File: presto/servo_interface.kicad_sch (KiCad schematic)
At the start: 0 parts

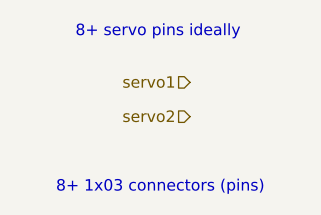
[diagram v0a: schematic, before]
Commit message: Minor document changes
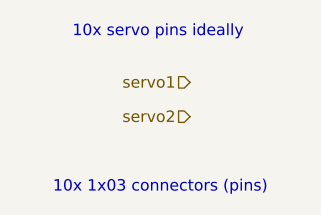
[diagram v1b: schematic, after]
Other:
- note added: "10x 1x03 connectors (pins)"
- note added: "10x servo pins ideally"
- note removed: "8+ 1x03 connectors (pins)"
- note removed: "8+ servo pins ideally"
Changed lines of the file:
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@@
 	(generator_version "9.0")
 	(paper "A4")
-	(text "8+ 1x03 connectors (pins)"
+	(text "10x 1x03 connectors (pins)"
 		(exclude_from_sim no)
 		(at 52.578 65.024 0)
@@
 		)
 	)
-	(text "8+ servo pins ideally\n"
+	(text "10x servo pins ideally\n"
 		(exclude_from_sim no)
 		(at 52.324 47.752 0)

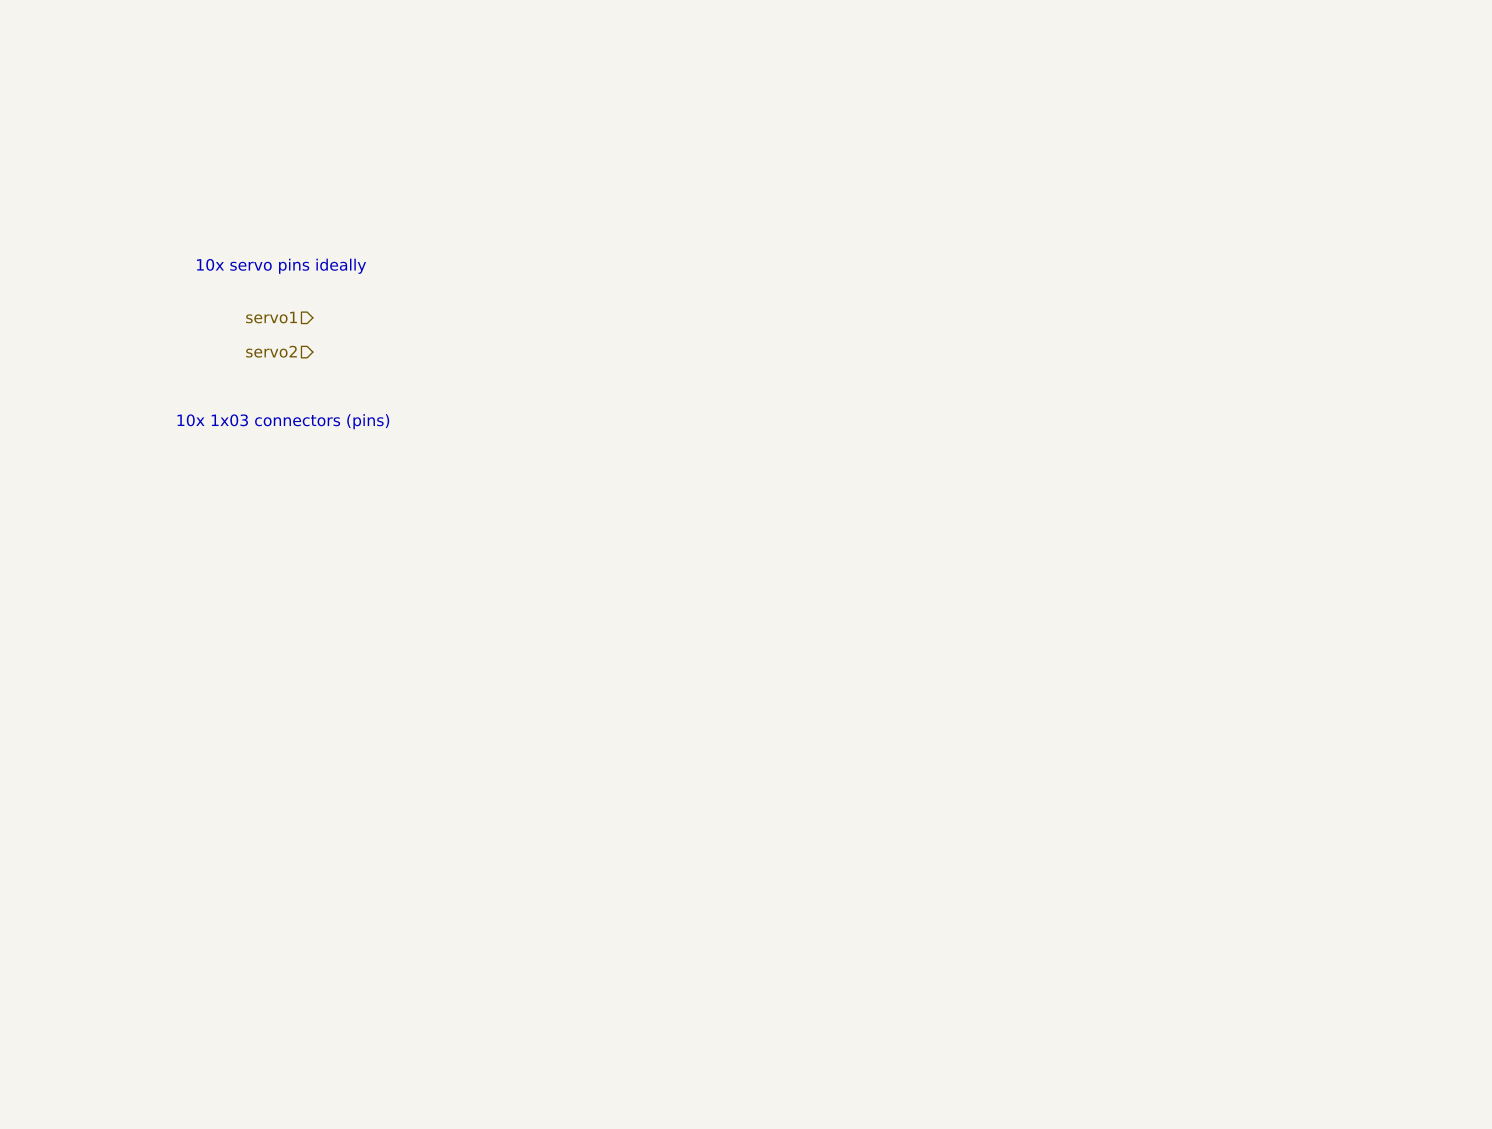
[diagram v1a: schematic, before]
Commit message: RC and Servo interface schematic done
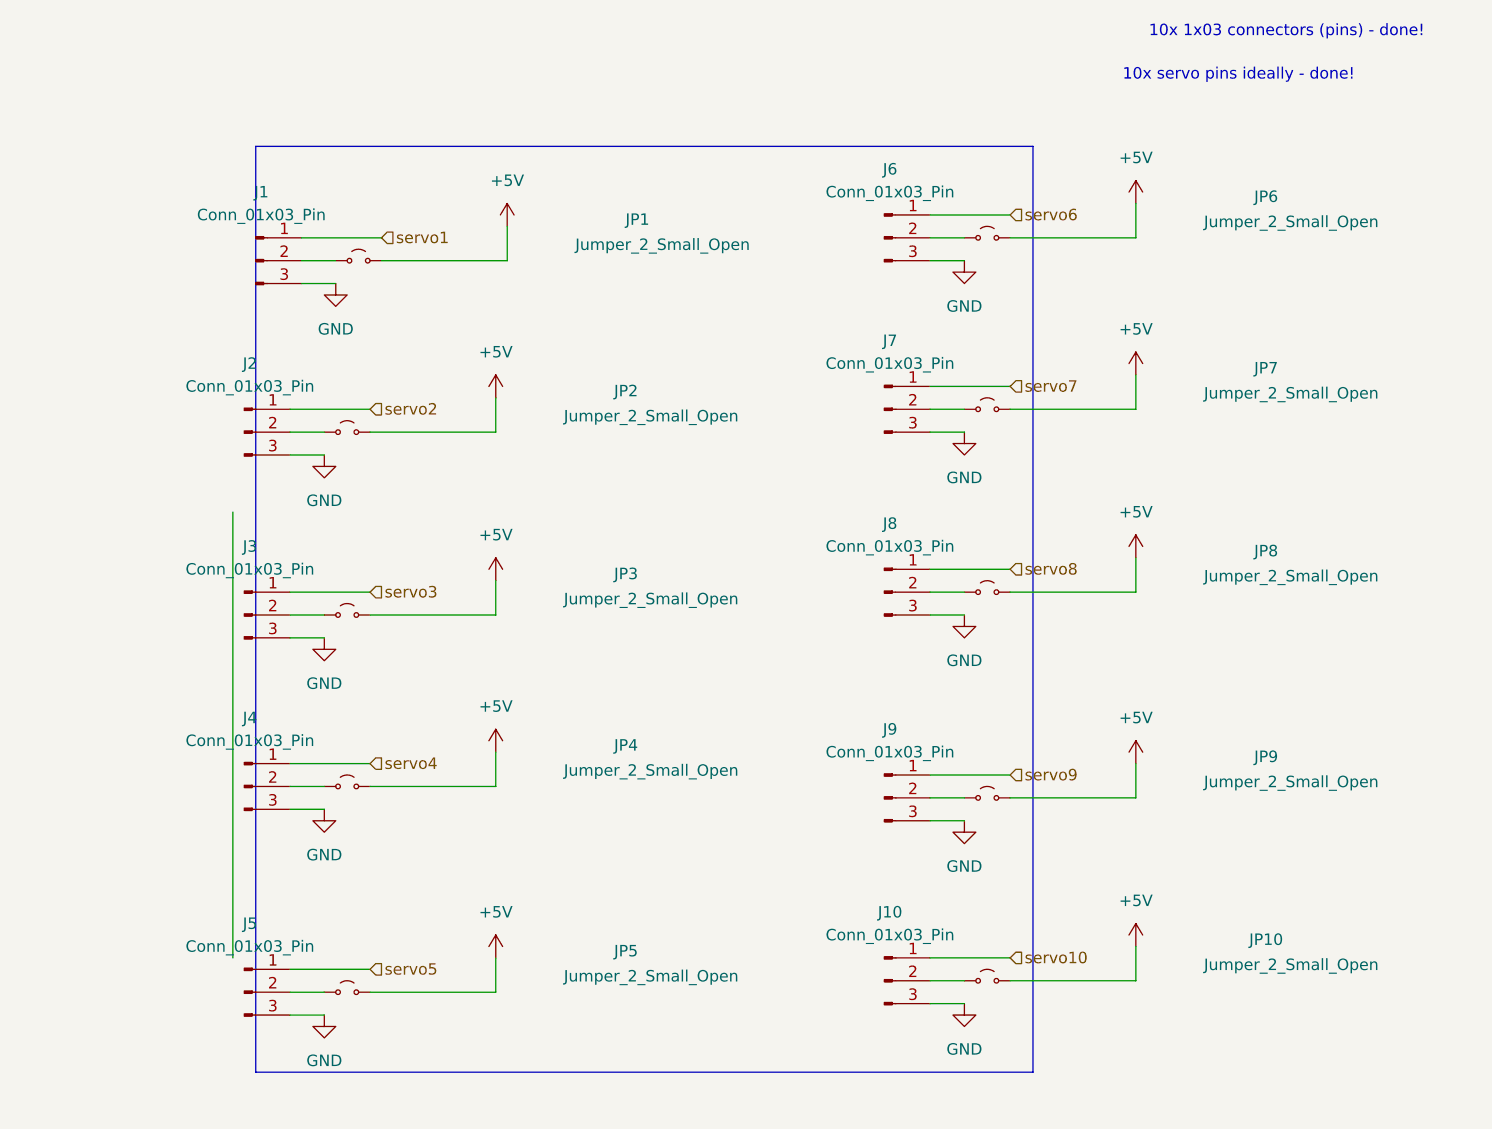
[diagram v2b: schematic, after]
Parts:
- added J1, J10, J2, J3, J4, J5, J6, J7, J8, J9: Conn_01x03_Pin, Connector_PinHeader_2.54mm:PinHeader_1x03_P2.54mm_Vertical, symbol Connector:Conn_01x03_Pin
- added JP1, JP10, JP2, JP3, JP4, JP5, JP6, JP7, JP8, JP9: Jumper_2_Small_Open, Jumper:SolderJumper-2_P1.3mm_Open_RoundedPad1.0x1.5mm, symbol Jumper:Jumper_2_Small_Open
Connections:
- net servo1: now also J1.1 (Pin_1)
- net servo2: now also J2.1 (Pin_1)
- new net: J10.2 (Pin_2), JP10.1 (A)
- new net: J8.2 (Pin_2), JP8.1 (A)
- new net: J9.2 (Pin_2), JP9.1 (A)
- new net: J3.2 (Pin_2), JP3.1 (A)
- new net: J2.2 (Pin_2), JP2.1 (A)
- new net: J6.2 (Pin_2), JP6.1 (A)
- new net: J7.2 (Pin_2), JP7.1 (A)
- new net: J4.2 (Pin_2), JP4.1 (A)
- new net: J1.2 (Pin_2), JP1.1 (A)
- new net: J5.2 (Pin_2), JP5.1 (A)
- new net +5V: JP1.2 (B), JP10.2 (B), JP2.2 (B), JP3.2 (B), JP4.2 (B), JP5.2 (B), JP6.2 (B), JP7.2 (B), JP8.2 (B), JP9.2 (B)
- new net GND: J1.3 (Pin_3), J10.3 (Pin_3), J2.3 (Pin_3), J3.3 (Pin_3), J4.3 (Pin_3), J5.3 (Pin_3), J6.3 (Pin_3), J7.3 (Pin_3), J8.3 (Pin_3), J9.3 (Pin_3)
- new net servo10: J10.1 (Pin_1)
- new net servo3: J3.1 (Pin_1)
- new net servo4: J4.1 (Pin_1)
- new net servo5: J5.1 (Pin_1)
- new net servo6: J6.1 (Pin_1)
- new net servo7: J7.1 (Pin_1)
- new net servo8: J8.1 (Pin_1)
- new net servo9: J9.1 (Pin_1)
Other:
- note added: "10x 1x03 connectors (pins) - done!"
- note added: "10x servo pins ideally - done!"
- note removed: "10x 1x03 connectors (pins)"
- note removed: "10x servo pins ideally"

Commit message: Added estop, power, led schematics
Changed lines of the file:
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@@
 	(paper "A4")
 	(rectangle
-		(start 49.53 34.29)
-		(end 135.89 137.16)
+		(start 23.114 30.988)
+		(end 180.34 141.478)
 		(stroke
 			(width 0)
@@
 		)
 		(stroke
-			(width 0)
-			(type default)
-		)
-	)
-	(wire
-		(pts
-			(xy 46.99 74.93) (xy 46.99 124.46)
-		)
-		(stroke

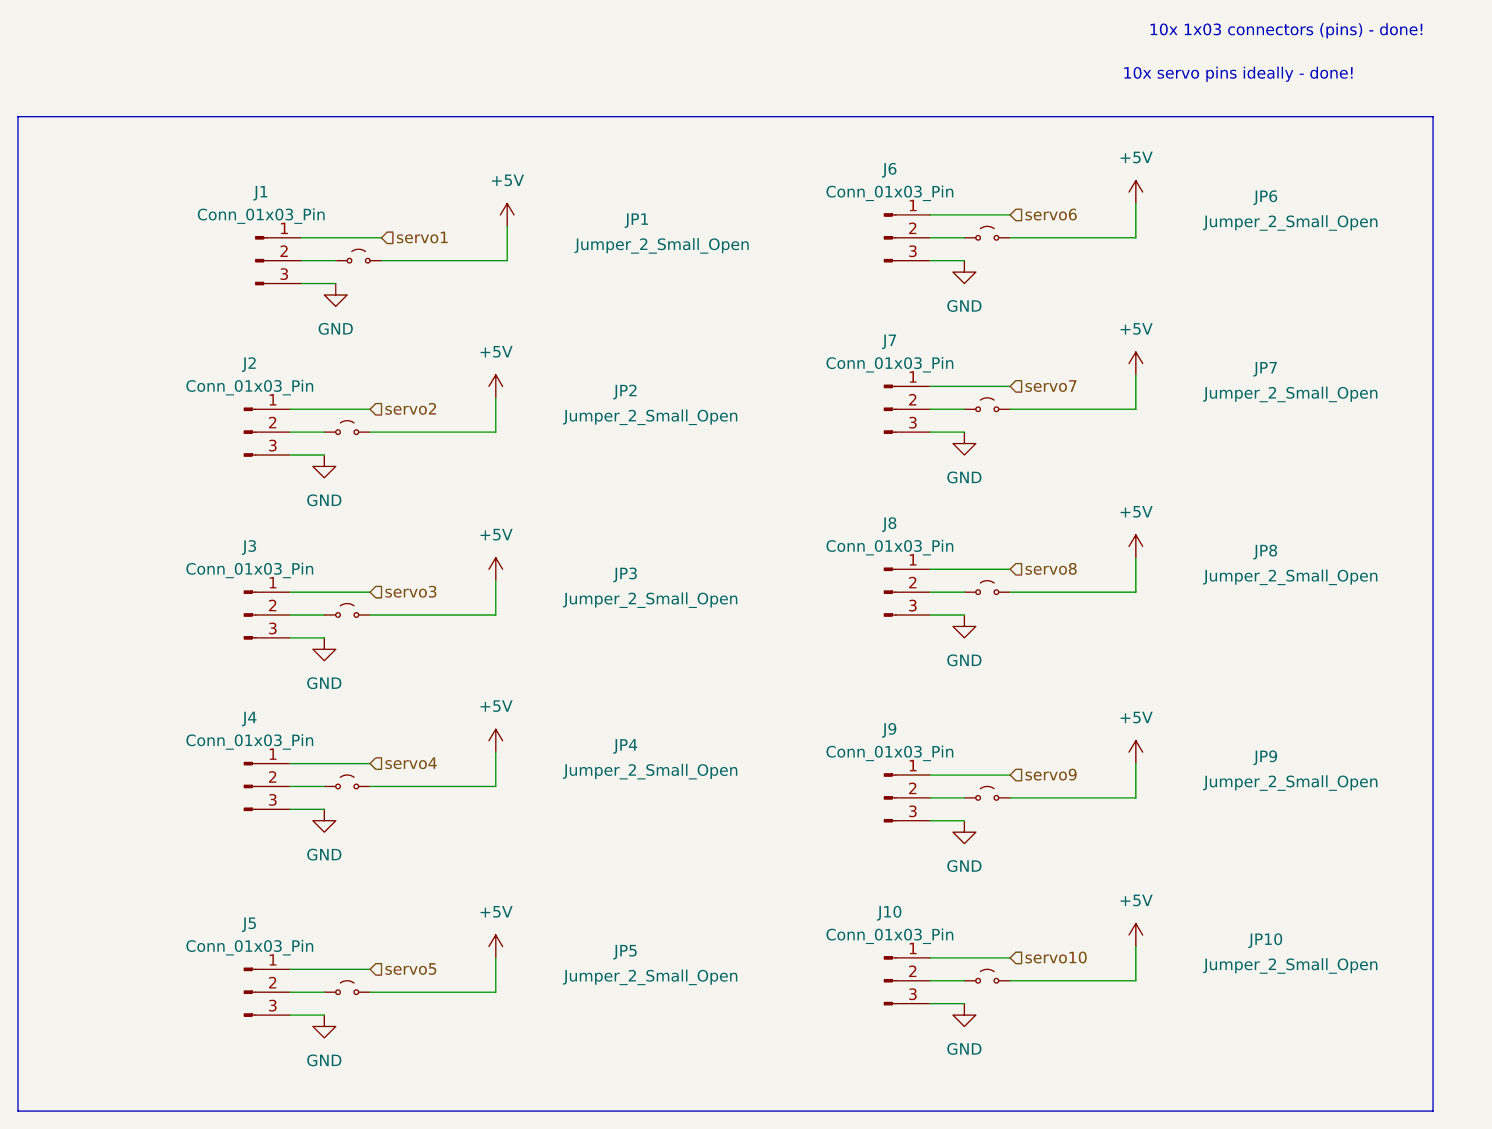
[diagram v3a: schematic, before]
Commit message: Presto PCB edited with schematic, components placed, wiring in progress
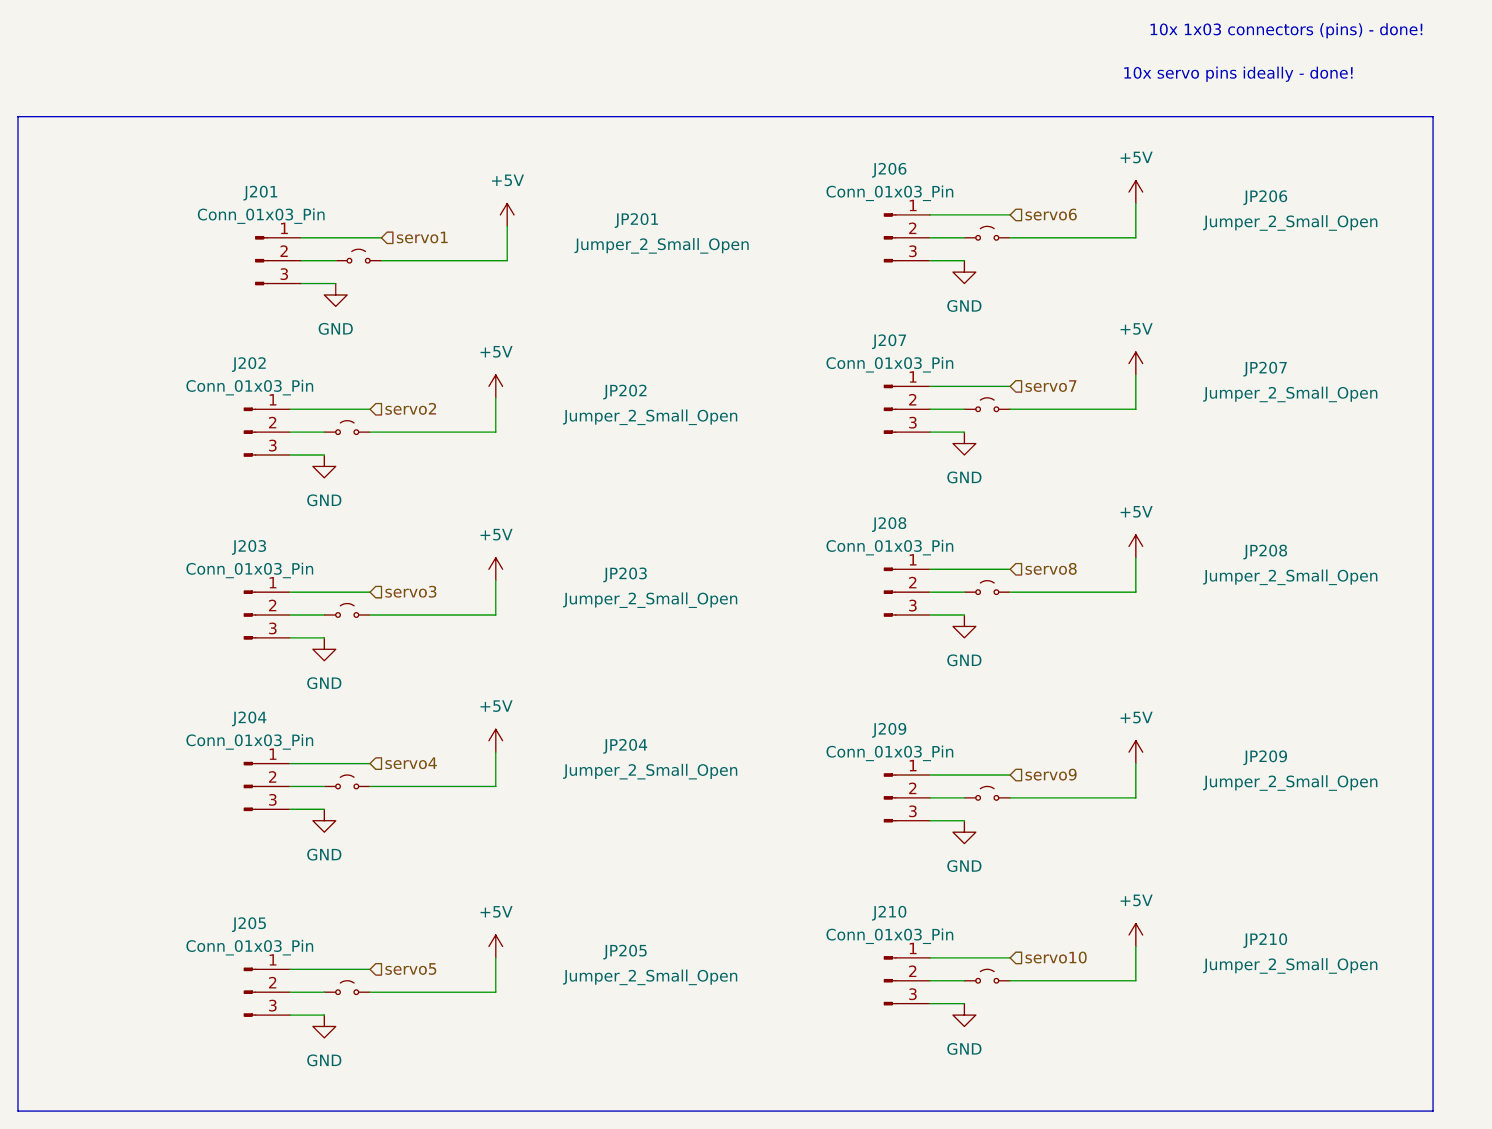
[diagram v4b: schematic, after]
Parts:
- renumbered J1 to J201, J2 to J202, J3 to J203, J4 to J204, J5 to J205, J6 to J206, J7 to J207, J8 to J208, J9 to J209, J10 to J210, JP1 to JP201, JP2 to JP202, JP3 to JP203, JP4 to JP204, JP5 to JP205, JP6 to JP206, JP7 to JP207, JP8 to JP208, JP9 to JP209, JP10 to JP210

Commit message: Rearranged to accomodate JST
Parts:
- J201, J202, J203, J204, J205, J206, J207, J208, J209, J210: footprint Connector_PinHeader_2.54mm:PinHeader_1x03_P2.54mm_Vertical -> Connector_JST:JST_XH_B3B-XH-A_1x03_P2.50mm_Vertical
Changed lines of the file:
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@@
 			)
 		)
-		(property "Footprint" "Connector_PinHeader_2.54mm:PinHeader_1x03_P2.54mm_Vertical"
+		(property "Footprint" "Connector_JST:JST_XH_B3B-XH-A_1x03_P2.50mm_Vertical"
 			(at 48.26 86.36 0)
 			(effects
@@
 			)
 		)
-		(property "Footprint" "Connector_PinHeader_2.54mm:PinHeader_1x03_P2.54mm_Vertical"
+		(property "Footprint" "Connector_JST:JST_XH_B3B-XH-A_1x03_P2.50mm_Vertical"
 			(at 48.26 66.04 0)
 			(effects
@@
 			)
 		)
-		(property "Footprint" "Connector_PinHeader_2.54mm:PinHeader_1x03_P2.54mm_Vertical"
+		(property "Footprint" "Connector_JST:JST_XH_B3B-XH-A_1x03_P2.50mm_Vertical"
 			(at 48.26 105.41 0)
 			(effects
@@
 			)
 		)
-		(property "Footprint" "Connector_PinHeader_2.54mm:PinHeader_1x03_P2.54mm_Vertical"
+		(property "Footprint" "Connector_JST:JST_XH_B3B-XH-A_1x03_P2.50mm_Vertical"
 			(at 49.53 46.99 0)
 			(effects
@@
 			)
 		)
-		(property "Footprint" "Connector_PinHeader_2.54mm:PinHeader_1x03_P2.54mm_Vertical"
+		(property "Footprint" "Connector_JST:JST_XH_B3B-XH-A_1x03_P2.50mm_Vertical"
 			(at 48.26 128.27 0)
 			(effects
@@
 			)
 		)
-		(property "Footprint" "Connector_PinHeader_2.54mm:PinHeader_1x03_P2.54mm_Vertical"
+		(property "Footprint" "Connector_JST:JST_XH_B3B-XH-A_1x03_P2.50mm_Vertical"
 			(at 119.38 44.45 0)
 			(effects
@@
 			)
 		)
-		(property "Footprint" "Connector_PinHeader_2.54mm:PinHeader_1x03_P2.54mm_Vertical"
+		(property "Footprint" "Connector_JST:JST_XH_B3B-XH-A_1x03_P2.50mm_Vertical"
 			(at 119.38 63.5 0)
 			(effects
@@
 			)
 		)
-		(property "Footprint" "Connector_PinHeader_2.54mm:PinHeader_1x03_P2.54mm_Vertical"
+		(property "Footprint" "Connector_JST:JST_XH_B3B-XH-A_1x03_P2.50mm_Vertical"
 			(at 119.38 106.68 0)
 			(effects
@@
 			)
 		)
-		(property "Footprint" "Connector_PinHeader_2.54mm:PinHeader_1x03_P2.54mm_Vertical"
+		(property "Footprint" "Connector_JST:JST_XH_B3B-XH-A_1x03_P2.50mm_Vertical"
 			(at 119.38 83.82 0)
 			(effects
@@
 			)
 		)
-		(property "Footprint" "Connector_PinHeader_2.54mm:PinHeader_1x03_P2.54mm_Vertical"
+		(property "Footprint" "Connector_JST:JST_XH_B3B-XH-A_1x03_P2.50mm_Vertical"
 			(at 119.38 127 0)
 			(effects
